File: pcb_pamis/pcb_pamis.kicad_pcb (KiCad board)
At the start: 4 copper layers, 79 x 100.5 mm, 60 parts, among them J1 USB_C_Receptacle_USB2.0_16P, J10 Conn_01x03, J11 Conn_01x03, J12 Conn_02x06_Odd_Even, J2 1755736, J3 Conn_01x04, J4 Conn_01x04, J5 Conn_01x04, J6 Conn_01x05, J7 Conn_01x05, J8 Conn_01x05, J9 Conn_01x03, Q1 Q_NPN_BEC, Q2 Q_NPN_BEC, SW1 SW_Push, U1 ESP32-WROOM-32UE, U2 CP2102N-Axx-xQFN28, U3 TMC2209_SILENTSTEPSTICK, U4 TMC2209_SILENTSTEPSTICK, U5 TMC2209_SILENTSTEPSTICK

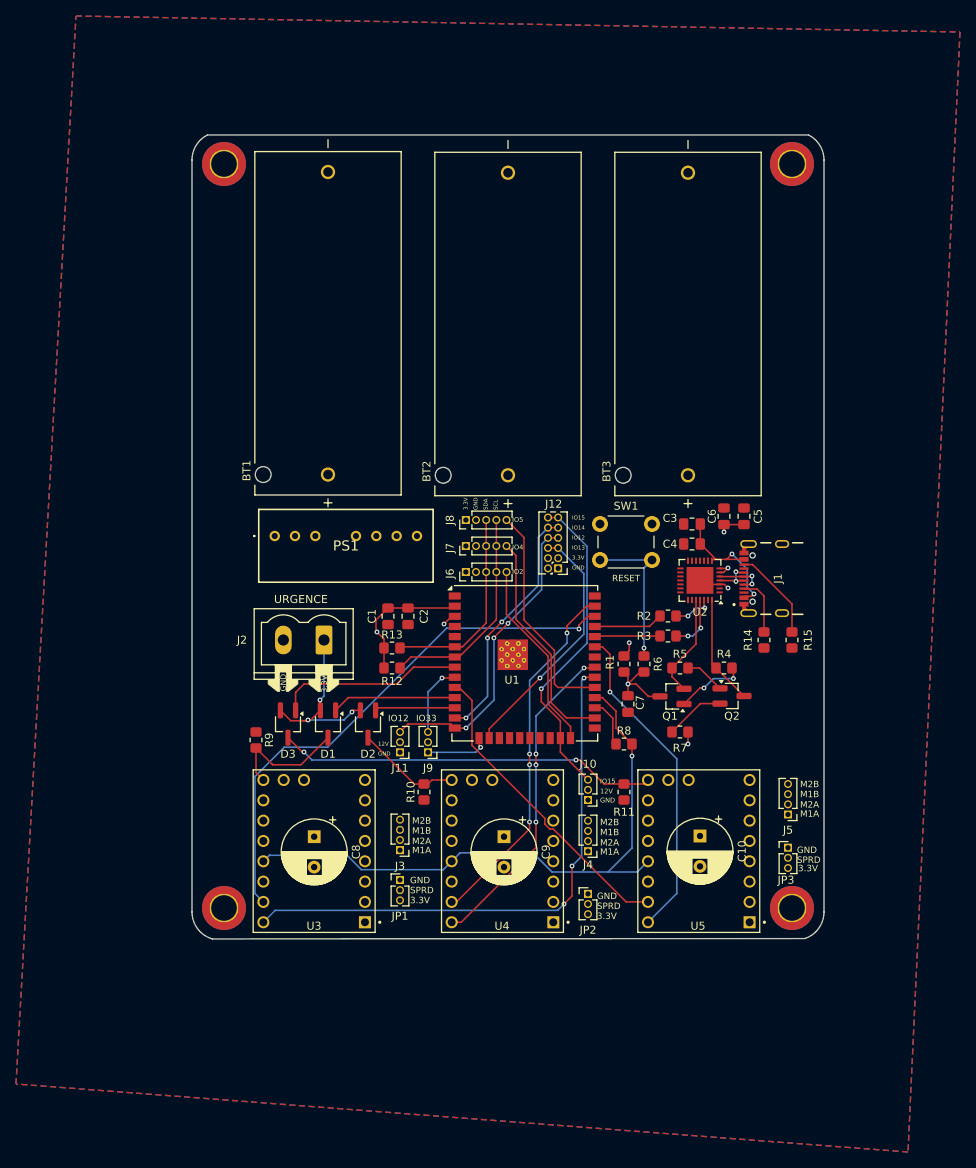
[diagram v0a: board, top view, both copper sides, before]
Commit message: commencement correctifs PCB Pami
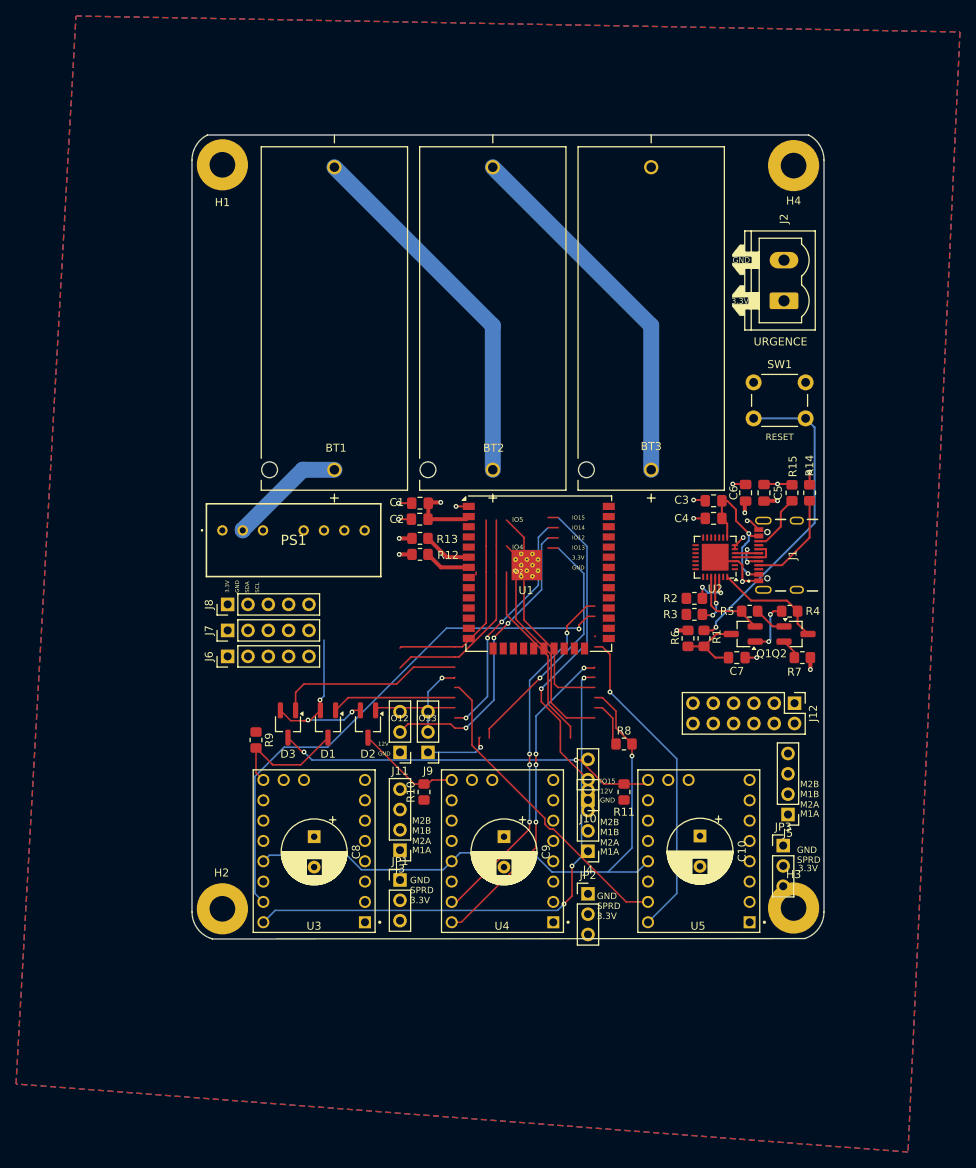
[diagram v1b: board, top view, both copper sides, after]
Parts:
- H1, H2, H3, H4: footprint MountingHole:MountingHole_3.2mm_M3_ISO14580_Pad_TopBottom -> MountingHole:MountingHole_3.2mm_M3_Pad
- J10, J11, J9, JP1, JP2, JP3: footprint Connector_PinHeader_1.27mm:PinHeader_1x03_P1.27mm_Vertical -> Connector_PinHeader_2.54mm:PinHeader_1x03_P2.54mm_Vertical
- J12: footprint Connector_PinHeader_1.27mm:PinHeader_2x06_P1.27mm_Vertical -> Connector_PinHeader_2.54mm:PinHeader_2x06_P2.54mm_Vertical
- J3, J4, J5: footprint Connector_PinHeader_1.27mm:PinHeader_1x04_P1.27mm_Vertical -> Connector_PinHeader_2.54mm:PinHeader_1x04_P2.54mm_Vertical
- J6, J7, J8: footprint Connector_PinHeader_1.27mm:PinHeader_1x05_P1.27mm_Vertical -> Connector_PinHeader_2.54mm:PinHeader_1x05_P2.54mm_Vertical
- moved J2 71.4 mm to (143.5, 48.6), turned to 90 degrees
- moved J12 34.0 mm to (144.8, 98.9), turned to -90 degrees
- moved J6 31.6 mm to (74.0, 93.0)
- moved J7 31.6 mm to (74.0, 89.8)
- moved J8 31.6 mm to (74.0, 86.5)
- moved SW1 26.1 mm to (139.7, 58.8)
- moved R14 19.3 mm to (146.7, 72.6), turned to 90 degrees
- moved R15 18.4 mm to (144.5, 72.6), turned to 90 degrees
- moved R7 17.9 mm to (145.8, 93.2)
- moved C7 14.8 mm to (137.6, 93.2), turned to 0 degrees
- moved C1 14.7 mm to (98.0, 73.9), turned to 180 degrees
- moved R12 14.6 mm to (98.0, 80.3)
- moved R13 14.1 mm to (98.0, 78.3)
- moved C2 12.2 mm to (98.0, 75.9), turned to 180 degrees
- moved Q1 11.8 mm to (138.4, 90.2)
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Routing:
- net VCC: track 172.5 -> 51.5 mm, vias 0 -> 3
- net EN: track 38.3 -> 9.68 mm, vias 2 -> 0
- net SCL: track 27.0 -> 5.77 mm
- net Net-(R1-Pad2): track 18.9 -> 39.8 mm
- net Net-(JP2-C): track 20.3 -> 0.00 mm
- net Net-(JP3-C): track 19.8 -> 0.00 mm
- net Net-(JP1-C): track 19.6 -> 0.00 mm
- net GND: track 15.8 -> 35.0 mm, vias 2 -> 12
- net SDA: track 24.9 -> 6.07 mm
- net Net-(J5-Pin_3): track 18.9 -> 0.50 mm
- net GPIO12/MISO: track 38.2 -> 53.2 mm, vias 3 -> 0
- net Net-(J3-Pin_3): track 10.1 -> 0.00 mm
- net Net-(J4-Pin_3): track 10.1 -> 0.00 mm
- net TXD: track 8.69 -> 0.00 mm
- net RXD: track 8.18 -> 0.11 mm
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
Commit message: nouveau placement -suite
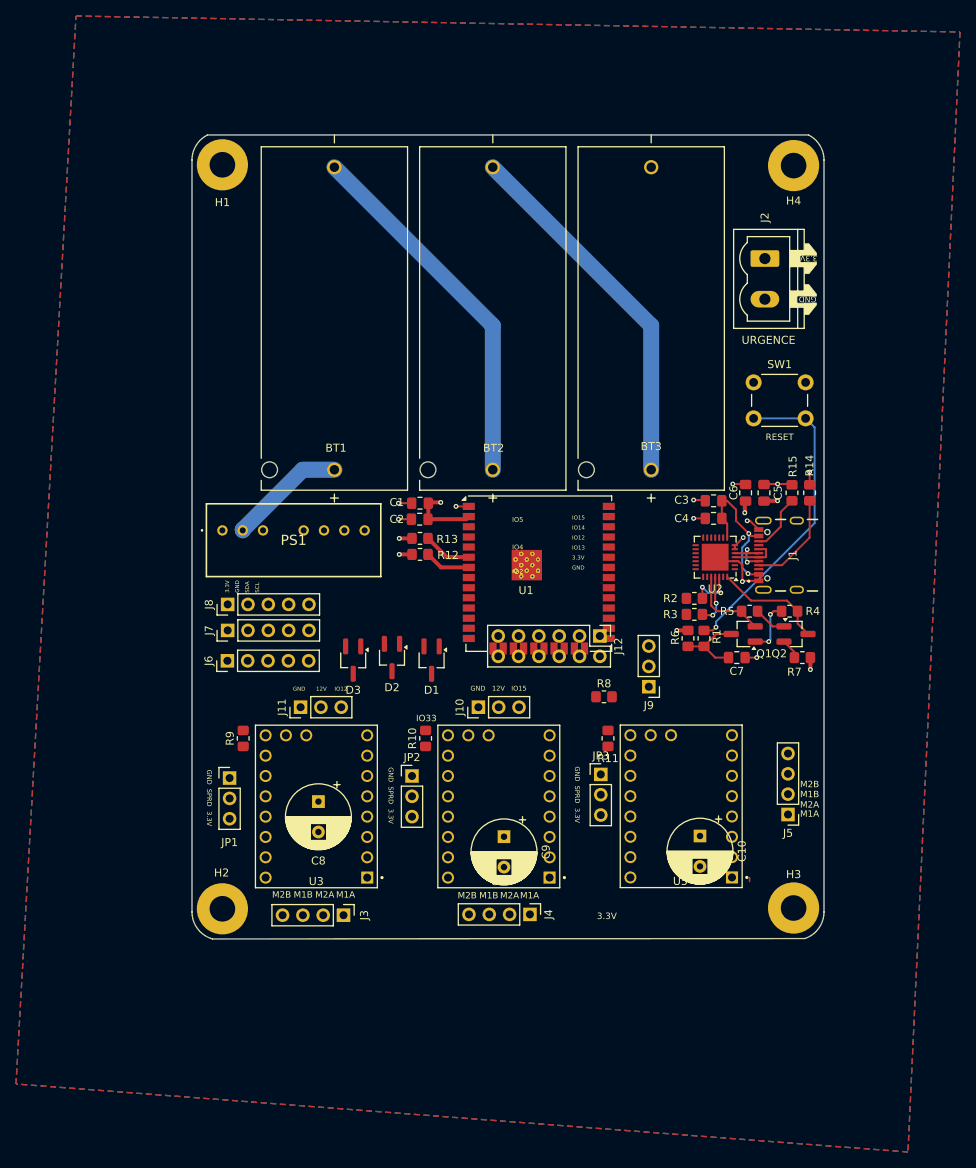
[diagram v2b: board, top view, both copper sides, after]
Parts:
- moved J9 28.8 mm to (126.6, 96.8)
- moved JP2 26.5 mm to (97.0, 108.0)
- moved J12 25.7 mm to (120.5, 90.5)
- moved JP1 24.8 mm to (74.2, 108.3)
- moved JP3 24.5 mm to (120.6, 107.8)
- moved J10 18.0 mm to (105.3, 99.4), turned to 90 degrees
- moved D1 15.2 mm to (99.5, 93.5)
- moved J11 13.6 mm to (83.1, 99.4), turned to 90 degrees
- moved D3 11.4 mm to (89.7, 93.5)
- moved J3 10.8 mm to (88.4, 125.4), turned to -90 degrees
- moved J4 10.7 mm to (111.7, 125.3), turned to -90 degrees
- moved D2 8.83 mm to (94.5, 93.2)
- moved R11 6.99 mm to (121.5, 103.3)
- moved R10 6.70 mm to (98.7, 103.3)
- moved R8 6.41 mm to (121.0, 98.1)
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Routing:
- net TX_MOTEUR: track 77.1 -> 0.00 mm, vias 1 -> 0
- net DIR1: track 69.2 -> 0.00 mm, vias 3 -> 0
- net STEP1: track 67.3 -> 0.00 mm, vias 1 -> 0
- net GPIO12/MISO: track 53.2 -> 0.00 mm
- net /Drivers moteurs pas à pas/DISA3: track 47.6 -> 0.00 mm, vias 2 -> 0
- net STEP2: track 45.3 -> 0.00 mm, vias 4 -> 0
- net DIR2: track 40.7 -> 0.00 mm, vias 4 -> 0
- net DIR3: track 40.7 -> 0.00 mm, vias 1 -> 0
- net GPIO15/CS: track 39.1 -> 0.00 mm, vias 1 -> 0
- net STEP3: track 39.0 -> 0.00 mm
- net VCC: track 51.5 -> 14.6 mm, vias 3 -> 0
- net GPIO13/MOSI: track 31.3 -> 0.00 mm, vias 1 -> 0
- net GPIO14/CLK: track 30.7 -> 0.00 mm, vias 3 -> 0
- net GPIO5: track 29.5 -> 0.00 mm
- net GPIO4: track 28.1 -> 0.00 mm
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
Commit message: finalisation nouveau routage
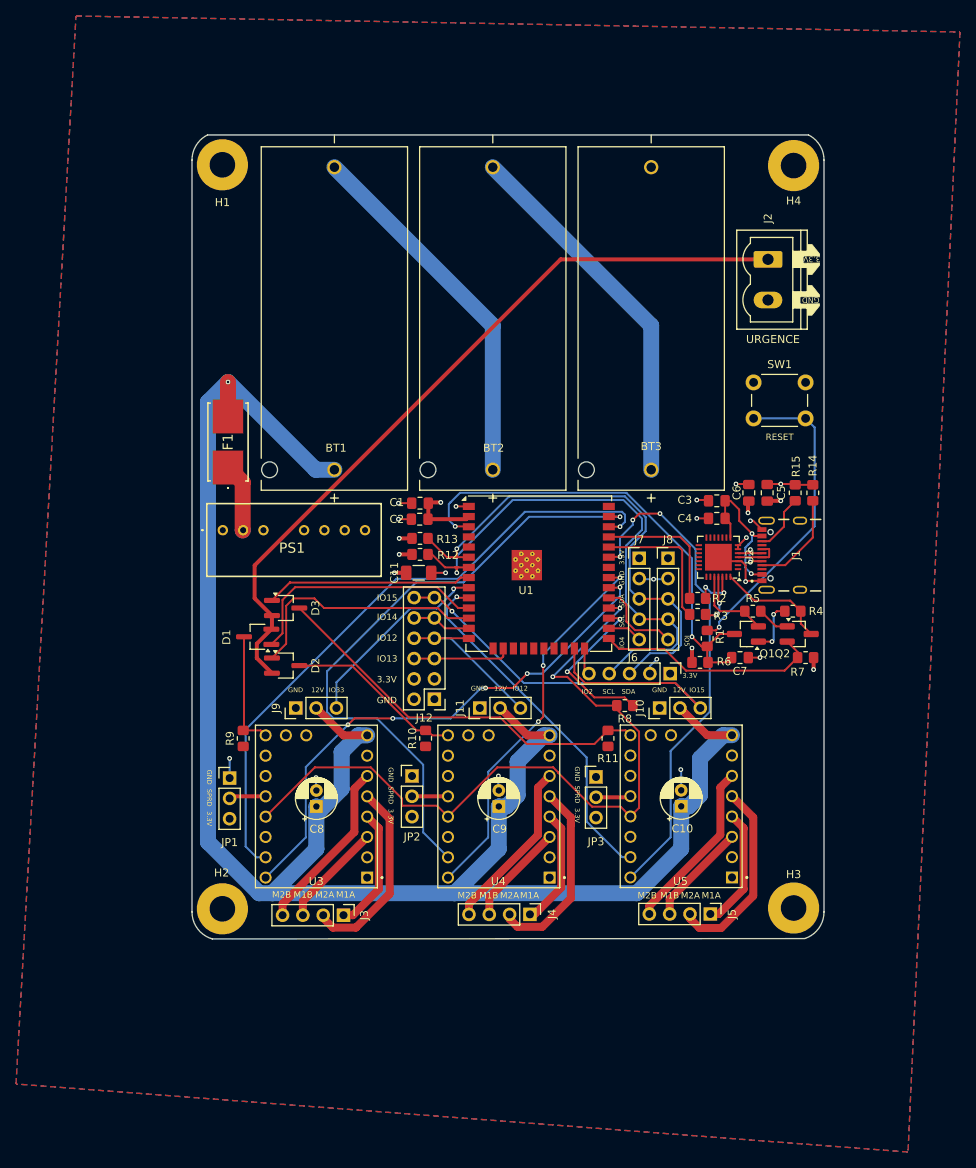
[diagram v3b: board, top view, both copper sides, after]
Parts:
- added C11: 100uF, Capacitor_SMD:C_1206_3216Metric_Pad1.33x1.80mm_HandSolder, F.Cu at (97.8, 82.6)
- added F1: 7A, Modelec:01550900M, F.Cu at (74.0, 66.2)
- C10, C8, C9: value 100uF 50V -> 100uF 16V; footprint Capacitor_THT:CP_Radial_D8.0mm_P3.80mm -> Capacitor_THT:CP_Radial_D5.0mm_P2.00mm
- moved J6 55.4 mm to (129.3, 95.2), turned to -90 degrees
- moved J8 55.3 mm to (129.0, 80.8), turned to 0 degrees
- moved J7 52.2 mm to (125.4, 80.8), turned to 0 degrees
- moved J9 44.2 mm to (82.5, 99.5), turned to 90 degrees
- moved J10 22.7 mm to (128.0, 99.5)
- moved J11 22.4 mm to (105.5, 99.5)
- moved J12 22.1 mm to (99.8, 98.4), turned to 180 degrees
- moved D1 21.9 mm to (77.7, 90.6), turned to 180 degrees
- moved J5 15.8 mm to (134.3, 125.2), turned to -90 degrees
- moved D2 13.3 mm to (81.2, 94.2), turned to 0 degrees
- moved D3 10.7 mm to (81.2, 87.0), turned to 0 degrees
- moved C10 4.39 mm to (130.7, 111.8), turned to 90 degrees
- moved C9 3.83 mm to (107.8, 111.8), turned to 90 degrees
- moved R6 3.35 mm to (133.0, 93.8), turned to 0 degrees
- moved R8 2.82 mm to (123.6, 99.2), turned to 180 degrees
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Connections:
- PS1 pad 2: VCC -> Net-(PS1-+VIN_(VCC))
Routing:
- net VCC: track 14.6 -> 238.0 mm, vias 0 -> 1
- net Net-(D1-A-Pad2): track 0.00 -> 96.0 mm
- net TX_MOTEUR: track 0.00 -> 94.5 mm, vias 0 -> 2
- net STEP1: track 0.00 -> 79.7 mm, vias 0 -> 1
- net STEP2: track 0.00 -> 78.7 mm, vias 0 -> 1
- net DIR1: track 0.00 -> 66.6 mm, vias 0 -> 5
- net DIR3: track 0.00 -> 62.6 mm, vias 0 -> 3
- net GPIO15/CS: track 0.00 -> 62.1 mm, vias 0 -> 1
- net SCL: track 5.77 -> 66.9 mm, vias 0 -> 1
- net SDA: track 6.07 -> 64.1 mm, vias 0 -> 1
- net EN: track 9.68 -> 60.9 mm, vias 0 -> 2
- net /Drivers moteurs pas à pas/DISA3: track 0.00 -> 49.4 mm
- net DIR2: track 0.00 -> 47.8 mm, vias 0 -> 3
- net STEP3: track 0.00 -> 44.7 mm, vias 0 -> 1
- net DISA2: track 0.00 -> 31.5 mm
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
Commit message: matrice de vias PCB Pami
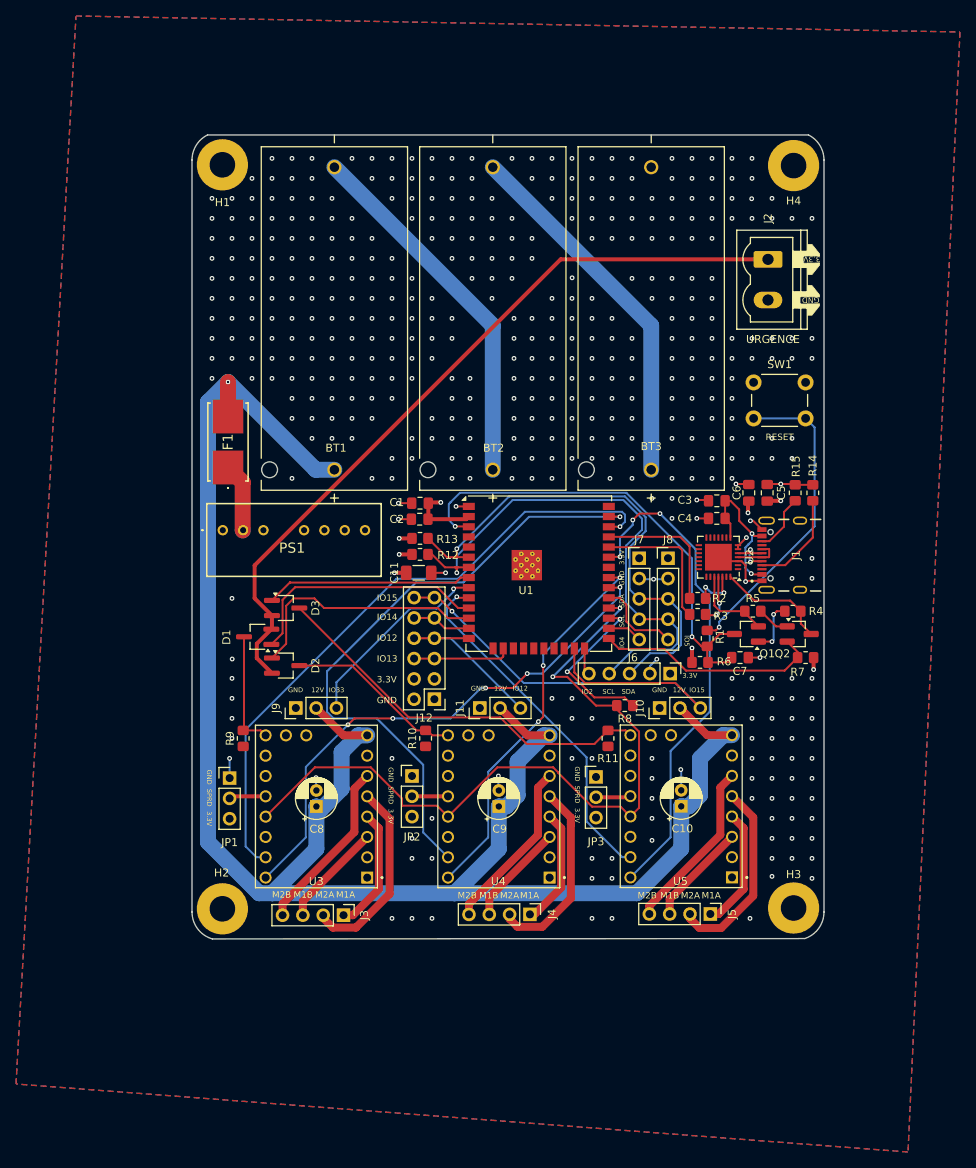
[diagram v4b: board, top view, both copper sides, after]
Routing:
- net GND: vias 17 -> 460
